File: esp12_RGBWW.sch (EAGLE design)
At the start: 36 parts, among them Q1 AOD2910SMD, Q2 AOD2910SMD, Q3 AOD2910SMD, Q4 AOD2910SMD, Q5 AOD2910SMD, U1 TPS5410DR

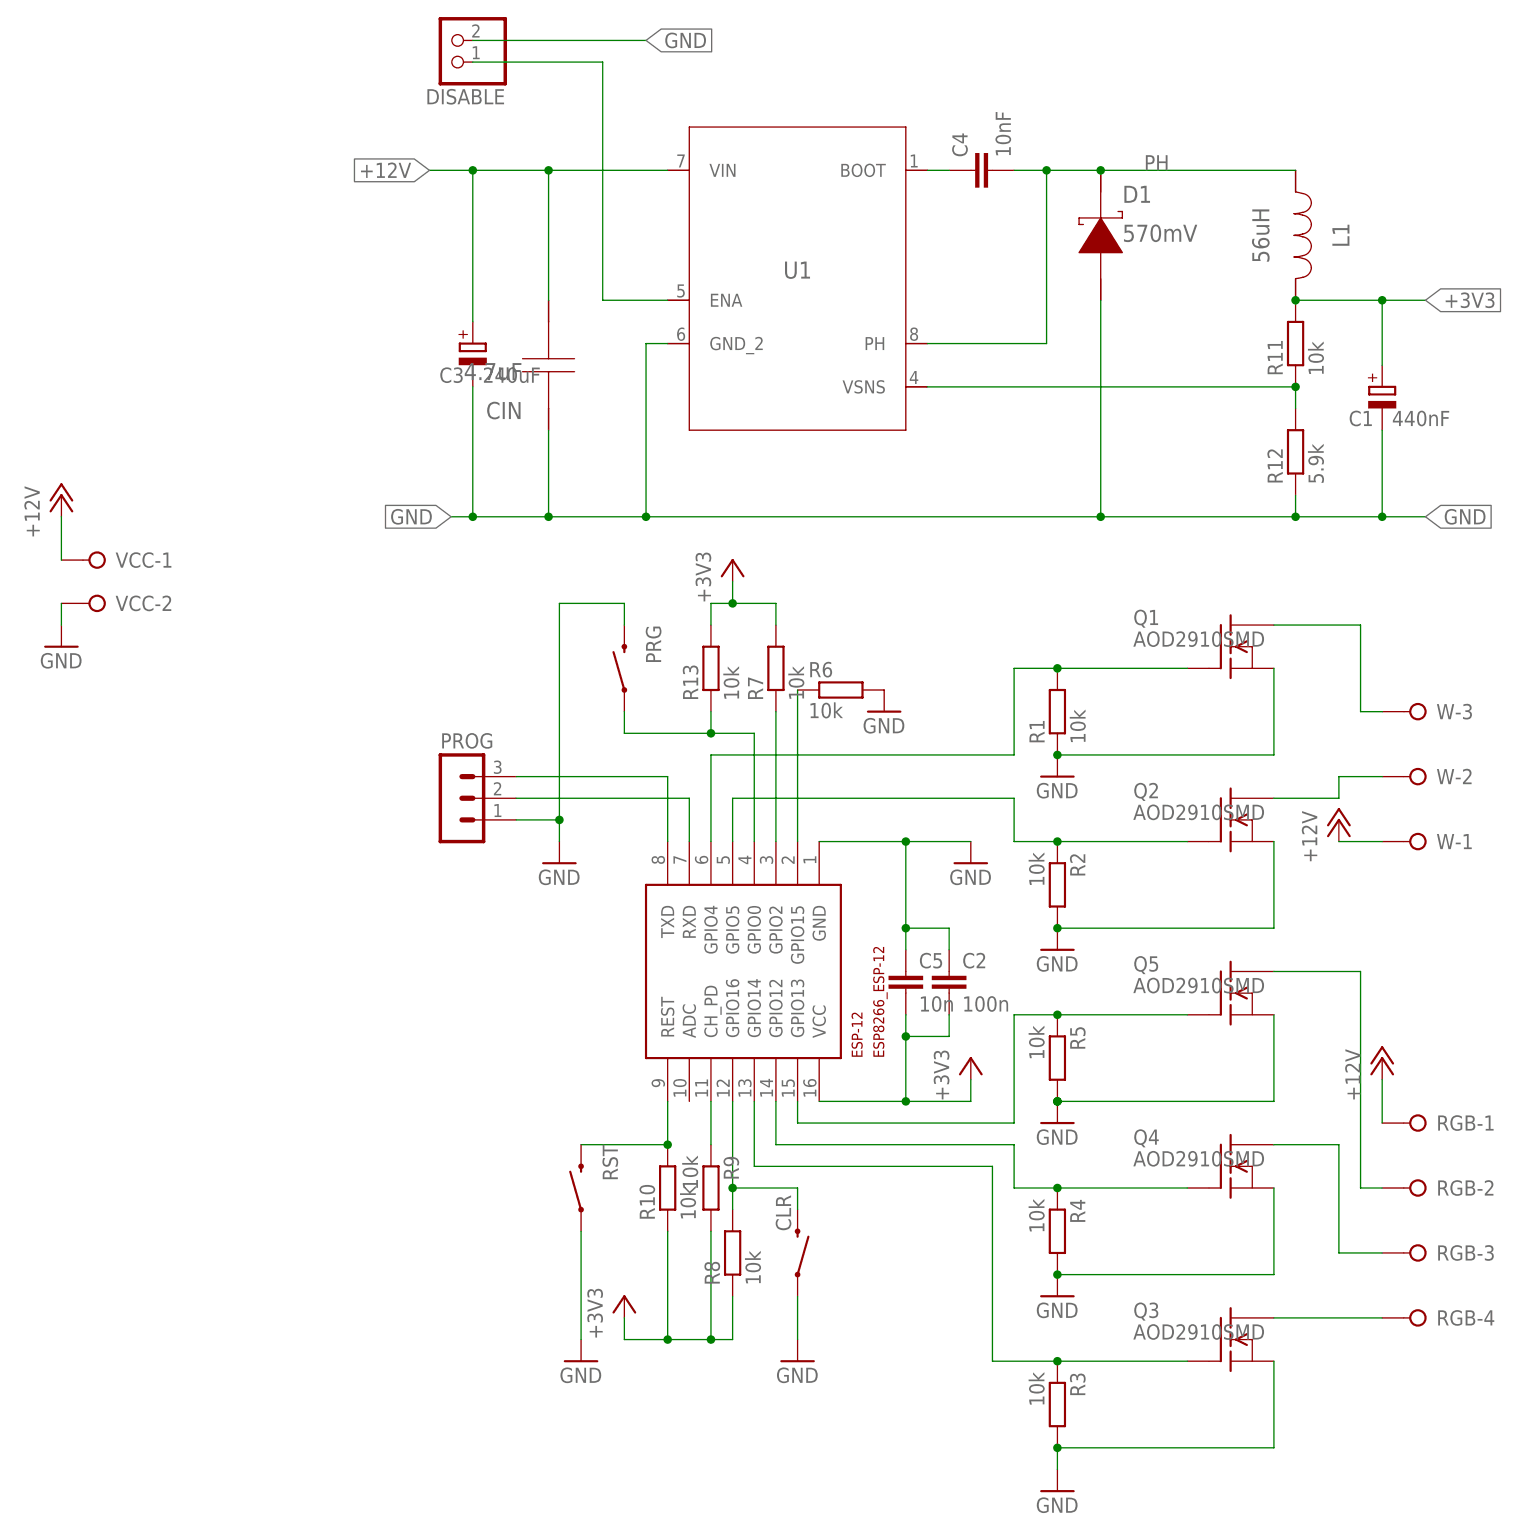
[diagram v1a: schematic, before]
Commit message: added three accessible GPIOs
Added header pins for GPIOS 0,2 and 16 (which are all pulled high on board).
If using Tasmota, or if we make changes to the "native" firmware, those can be used to signal via MQTT and thus to provide "local" control
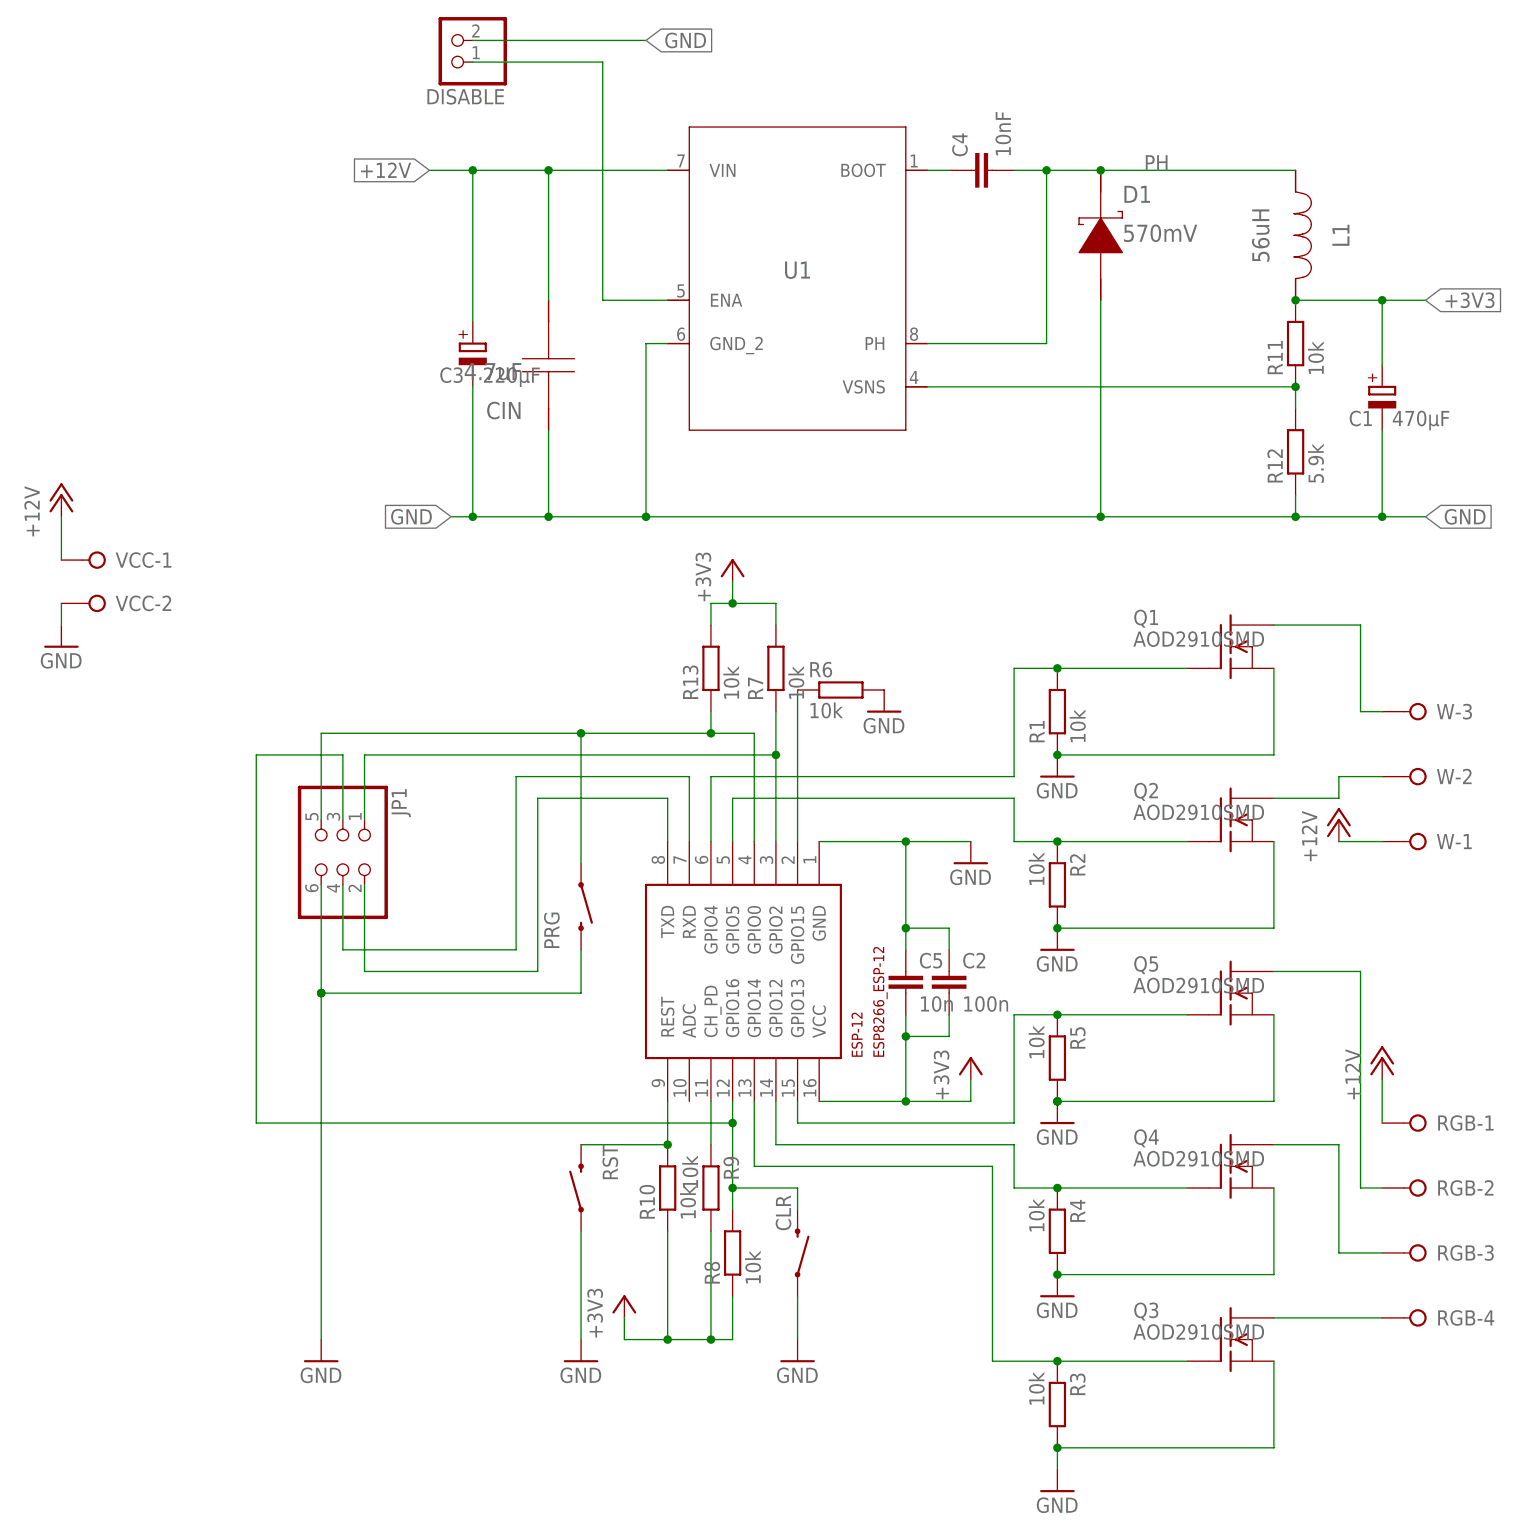
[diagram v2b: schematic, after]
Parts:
- removed PROG: (no value), con-lstb:MA03-1
- added JP1: (no value), adafruit:PINHD-2X3
- C1: value 440nF -> 470µF
- C3: value 240uF -> 220µF
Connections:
- net CLR_S: now also JP1.3
- net G2: now also JP1.1
- net GND: now also JP1.6; no longer PROG.1
- net PRG_S: now also JP1.5
- net RXD: now also JP1.4; no longer PROG.2
- net TXD: now also JP1.2; no longer PROG.3
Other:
- moved on the sheet: PRG
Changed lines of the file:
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@@
 <part name="R8" library="rcl" deviceset="R-EU_" device="R0805" value="10k"/>
 <part name="GND14" library="supply1" deviceset="GND" device=""/>
-<part name="C1" library="resistor" deviceset="CPOL-EU" device="E2.5-7" value="440nF"/>
+<part name="C1" library="resistor" deviceset="CPOL-EU" device="E2.5-7" value="470µF"/>
 <part name="CIN" library="AcceleratedDesigns_Lib" deviceset="GRM31CR71H475KA12L" device="" value="4.7uF"/>
 <part name="D1" library="TI_Accelerated_Design_neu" deviceset="B160-13-F" device="" value="570mV"/>
@@
 <part name="Q4" library="transistor-fet+irf7201" deviceset="AOD2910" device="" technology="SMD"/>
 <part name="Q3" library="transistor-fet+irf7201" deviceset="AOD2910" device="" technology="SMD"/>
-<part name="C3" library="resistor" deviceset="CPOL-EU" device="E2.5-7" value="240uF"/>
-<part name="PROG" library="con-lstb" deviceset="MA03-1" device=""/>
+<part name="C3" library="resistor" deviceset="CPOL-EU" device="E2.5-7" value="220µF"/>
 <part name="C5" library="rcl" deviceset="C-EU" device="C0805" value="10n"/>
 <part name="DISABLE" library="pinhead" deviceset="PINHD-1X2" device=""/>
+<part name="JP1" library="adafruit" deviceset="PINHD-2X3" device=""/>
 </parts>
 <sheets>
@@
 <instance part="GND12" gate="1" x="53.34" y="60.96"/>
 <instance part="+3V4" gate="G$1" x="22.86" y="-7.62"/>
-<instance part="GND13" gate="1" x="15.24" y="43.18"/>
+<instance part="GND13" gate="1" x="-12.7" y="-15.24"/>
 <instance part="R10" gate="G$1" x="27.94" y="5.08" rot="R90"/>
 <instance part="C2" gate="G$1" x="60.96" y="30.48"/>
@@
 <instance part="R12" gate="G$1" x="101.6" y="91.44" rot="R90"/>
 <instance part="C4" gate="G$1" x="63.5" y="124.46" rot="R90"/>
-<instance part="PRG" gate="G$1" x="22.86" y="66.04" smashed="yes" rot="R90">
-<attribute name="NAME" x="25.4" y="71.12" size="1.778" layer="95" rot="R270"/>
-<attribute name="VALUE" x="25.4" y="63.5" size="1.778" layer="96" rot="R90"/>
+<instance part="PRG" gate="G$1" x="17.78" y="38.1" smashed="yes" rot="R270">
+<attribute name="NAME" x="15.24" y="33.02" size="1.778" layer="95" rot="R90"/>
+<attribute name="VALUE" x="15.24" y="40.64" size="1.778" layer="96" rot="R270"/>
 </instance>
 <instance part="R13" gate="G$1" x="33.02" y="66.04" rot="R90"/>
@@
 <attribute name="VALUE" x="6.223" y="99.5426" size="1.778" layer="96"/>
 </instance>
-<instance part="PROG" gate="G$1" x="2.54" y="50.8"/>
 <instance part="C5" gate="G$1" x="55.88" y="30.48"/>
 <instance part="DISABLE" gate="G$1" x="2.54" y="139.7" rot="R180"/>
+<instance part="JP1" gate="G$1" x="-12.7" y="45.72" rot="R270"/>
 </instances>
 <busses>
@@
 <pinref part="R7" gate="G$1" pin="1"/>
 <pinref part="ESP-12" gate="G$1" pin="GPIO2"/>
-<wire x1="40.64" y1="45.72" x2="40.64" y2="60.96" width="0.1524" layer="91"/>
+<wire x1="40.64" y1="45.72" x2="40.64" y2="55.88" width="0.1524" layer="91"/>
+<wire x1="40.64" y1="55.88" x2="40.64" y2="60.96" width="0.1524" layer="91"/>
+<wire x1="40.64" y1="55.88" x2="-7.62" y2="55.88" width="0.1524" layer="91"/>
+<junction x="40.64" y="55.88"/>
+<pinref part="JP1" gate="G$1" pin="1"/>
+<wire x1="-7.62" y1="48.26" x2="-7.62" y2="55.88" width="0.1524" layer="91"/>
 </segment>
 </net>
@@
 <wire x1="33.02" y1="58.42" x2="33.02" y2="60.96" width="0.1524" layer="91"/>
 <pinref part="PRG" gate="G$1" pin="1"/>
-<wire x1="33.02" y1="58.42" x2="22.86" y2="58.42" width="0.1524" layer="91"/>
-<wire x1="22.86" y1="60.96" x2="22.86" y2="58.42" width="0.1524" layer="91"/>
+<wire x1="33.02" y1="58.42" x2="17.78" y2="58.42" width="0.1524" layer="91"/>
+<wire x1="17.78" y1="43.18" x2="17.78" y2="58.42" width="0.1524" layer="91"/>
 <junction x="33.02" y="58.42"/>
+<wire x1="17.78" y1="58.42" x2="-12.7" y2="58.42" width="0.1524" layer="91"/>
+<junction x="17.78" y="58.42"/>
+<pinref part="JP1" gate="G$1" pin="5"/>
+<wire x1="-12.7" y1="58.42" x2="-12.7" y2="48.26" width="0.1524" layer="91"/>
 </segment>
 </net>
@@
 <segment>
 <pinref part="GND13" gate="1" pin="GND"/>
-<wire x1="15.24" y1="45.72" x2="15.24" y2="48.26" width="0.1524" layer="91"/>
+<wire x1="-12.7" y1="-12.7" x2="-12.7" y2="27.94" width="0.1524" layer="91"/>
 <pinref part="PRG" gate="G$1" pin="2"/>
-<wire x1="15.24" y1="48.26" x2="15.24" y2="73.66" width="0.1524" layer="91"/>
-<wire x1="15.24" y1="73.66" x2="22.86" y2="73.66" width="0.1524" layer="91"/>
-<wire x1="22.86" y1="73.66" x2="22.86" y2="71.12" width="0.1524" layer="91"/>
-<pinref part="PROG" gate="G$1" pin="1"/>
-<wire x1="10.16" y1="48.26" x2="15.24" y2="48.26" width="0.1524" layer="91"/>
-<junction x="15.24" y="48.26"/>
+<wire x1="-12.7" y1="27.94" x2="17.78" y2="27.94" width="0.1524" layer="91"/>
+<wire x1="17.78" y1="27.94" x2="17.78" y2="33.02" width="0.1524" layer="91"/>
+<pinref part="JP1" gate="G$1" pin="6"/>
+<wire x1="-12.7" y1="27.94" x2="-12.7" y2="40.64" width="0.1524" layer="91"/>
+<junction x="-12.7" y="27.94"/>
+<junction x="-12.7" y="27.94"/>
 </segment>
 <segment>
@@
 <segment>
 <pinref part="ESP-12" gate="G$1" pin="RXD"/>
-<wire x1="30.48" y1="50.8" x2="30.48" y2="45.72" width="0.1524" layer="91"/>
-<pinref part="PROG" gate="G$1" pin="2"/>
-<wire x1="10.16" y1="50.8" x2="30.48" y2="50.8" width="0.1524" layer="91"/>
+<wire x1="30.48" y1="53.34" x2="30.48" y2="45.72" width="0.1524" layer="91"/>
+<wire x1="10.16" y1="53.34" x2="30.48" y2="53.34" width="0.1524" layer="91"/>
+<wire x1="-10.16" y1="33.02" x2="10.16" y2="33.02" width="0.1524" layer="91"/>
+<wire x1="10.16" y1="33.02" x2="10.16" y2="53.34" width="0.1524" layer="91"/>
+<pinref part="JP1" gate="G$1" pin="4"/>
+<wire x1="-10.16" y1="33.02" x2="-10.16" y2="40.64" width="0.1524" layer="91"/>
 </segment>
 </net>
@@
 <segment>
 <pinref part="ESP-12" gate="G$1" pin="TXD"/>
-<pinref part="PROG" gate="G$1" pin="3"/>
-<wire x1="10.16" y1="53.34" x2="27.94" y2="53.34" width="0.1524" layer="91"/>
-<wire x1="27.94" y1="53.34" x2="27.94" y2="45.72" width="0.1524" layer="91"/>
+<wire x1="27.94" y1="50.8" x2="27.94" y2="45.72" width="0.1524" layer="91"/>
+<wire x1="-7.62" y1="30.48" x2="12.7" y2="30.48" width="0.1524" layer="91"/>
+<wire x1="12.7" y1="30.48" x2="12.7" y2="50.8" width="0.1524" layer="91"/>
+<wire x1="27.94" y1="50.8" x2="12.7" y2="50.8" width="0.1524" layer="91"/>
+<pinref part="JP1" gate="G$1" pin="2"/>
+<wire x1="-7.62" y1="30.48" x2="-7.62" y2="40.64" width="0.1524" layer="91"/>
 </segment>
 </net>
@@
 <segment>
 <pinref part="ESP-12" gate="G$1" pin="GPIO4"/>
-<wire x1="33.02" y1="45.72" x2="33.02" y2="55.88" width="0.1524" layer="91"/>
-<wire x1="33.02" y1="55.88" x2="68.58" y2="55.88" width="0.1524" layer="91"/>
+<wire x1="33.02" y1="45.72" x2="33.02" y2="53.34" width="0.1524" layer="91"/>
+<wire x1="33.02" y1="53.34" x2="68.58" y2="53.34" width="0.1524" layer="91"/>
 <wire x1="68.58" y1="66.04" x2="73.66" y2="66.04" width="0.1524" layer="91"/>
 <pinref part="R1" gate="G$1" pin="2"/>
-<wire x1="68.58" y1="66.04" x2="68.58" y2="55.88" width="0.1524" layer="91"/>
+<wire x1="68.58" y1="66.04" x2="68.58" y2="53.34" width="0.1524" layer="91"/>
 <wire x1="73.66" y1="66.04" x2="88.9" y2="66.04" width="0.1524" layer="91"/>
 <junction x="73.66" y="66.04"/>
@@
 <pinref part="ESP-12" gate="G$1" pin="GPIO16"/>
 <pinref part="R8" gate="G$1" pin="2"/>
-<wire x1="35.56" y1="15.24" x2="35.56" y2="5.08" width="0.1524" layer="91"/>
+<wire x1="35.56" y1="15.24" x2="35.56" y2="12.7" width="0.1524" layer="91"/>
 <pinref part="CLR" gate="G$1" pin="2"/>
+<wire x1="35.56" y1="12.7" x2="35.56" y2="5.08" width="0.1524" layer="91"/>
 <wire x1="35.56" y1="5.08" x2="35.56" y2="2.54" width="0.1524" layer="91"/>
 <wire x1="35.56" y1="5.08" x2="43.18" y2="5.08" width="0.1524" layer="91"/>
 <wire x1="43.18" y1="5.08" x2="43.18" y2="2.54" width="0.1524" layer="91"/>
 <junction x="35.56" y="5.08"/>
-</segment>
-</net>
+<wire x1="35.56" y1="12.7" x2="-20.32" y2="12.7" width="0.1524" layer="91"/>
+<wire x1="-20.32" y1="12.7" x2="-20.32" y2="55.88" width="0.1524" layer="91"/>
+<wire x1="-20.32" y1="55.88" x2="-10.16" y2="55.88" width="0.1524" layer="91"/>
+<junction x="35.56" y="12.7"/>
+<pinref part="JP1" gate="G$1" pin="3"/>
+<wire x1="-10.16" y1="55.88" x2="-10.16" y2="48.26" width="0.1524" layer="91"/>
+</segment>
+</net>
